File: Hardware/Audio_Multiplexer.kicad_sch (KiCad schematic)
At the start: 1 part

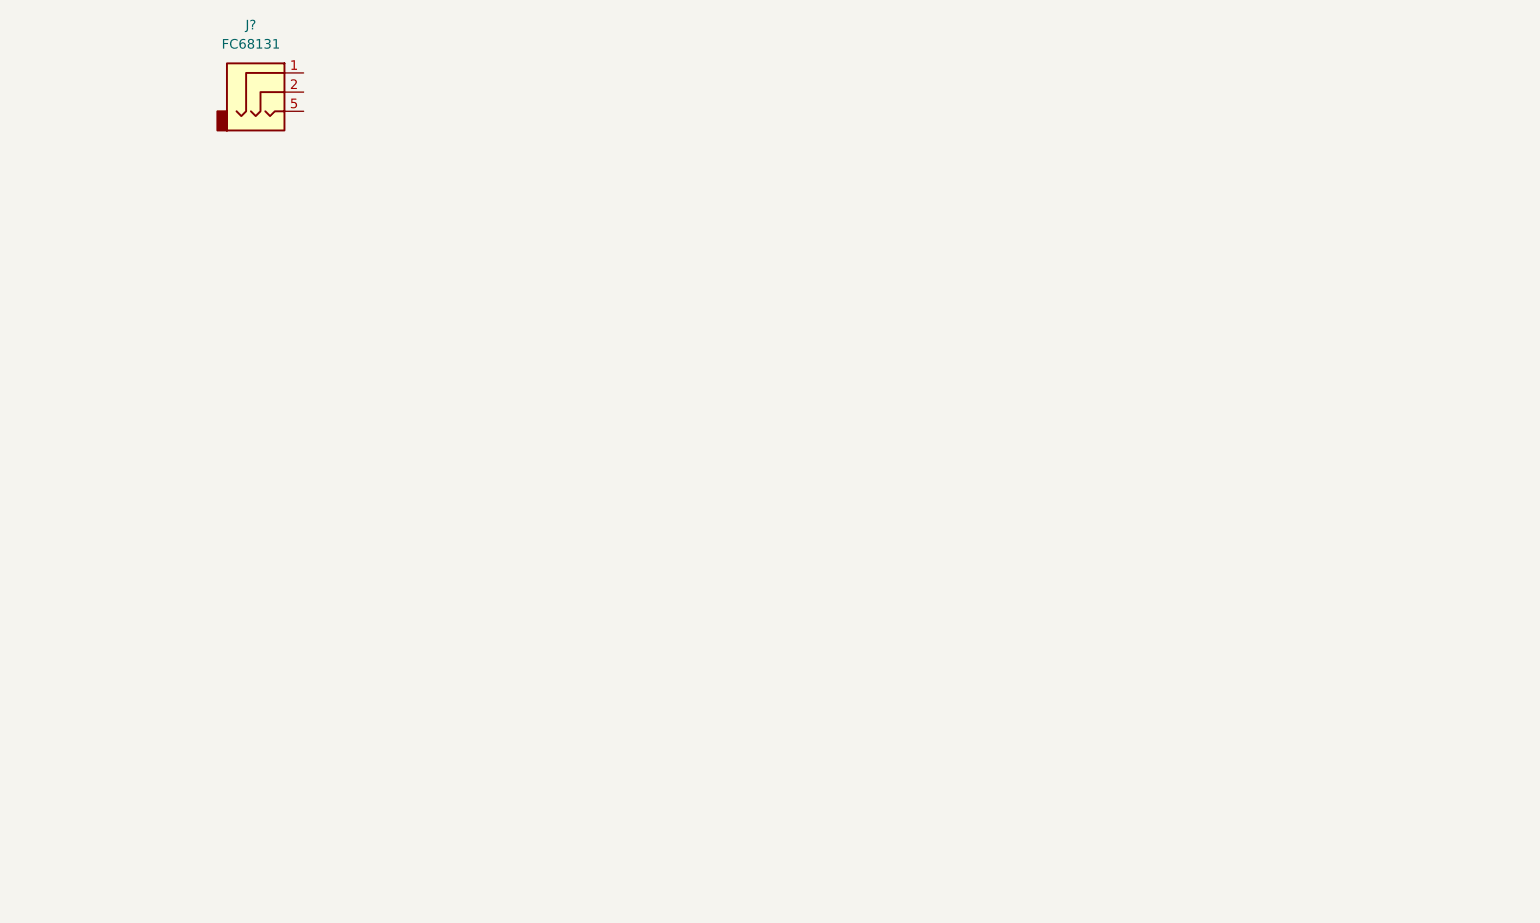
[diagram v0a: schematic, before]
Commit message: Finished schematic. Added audio and microphone blocks.
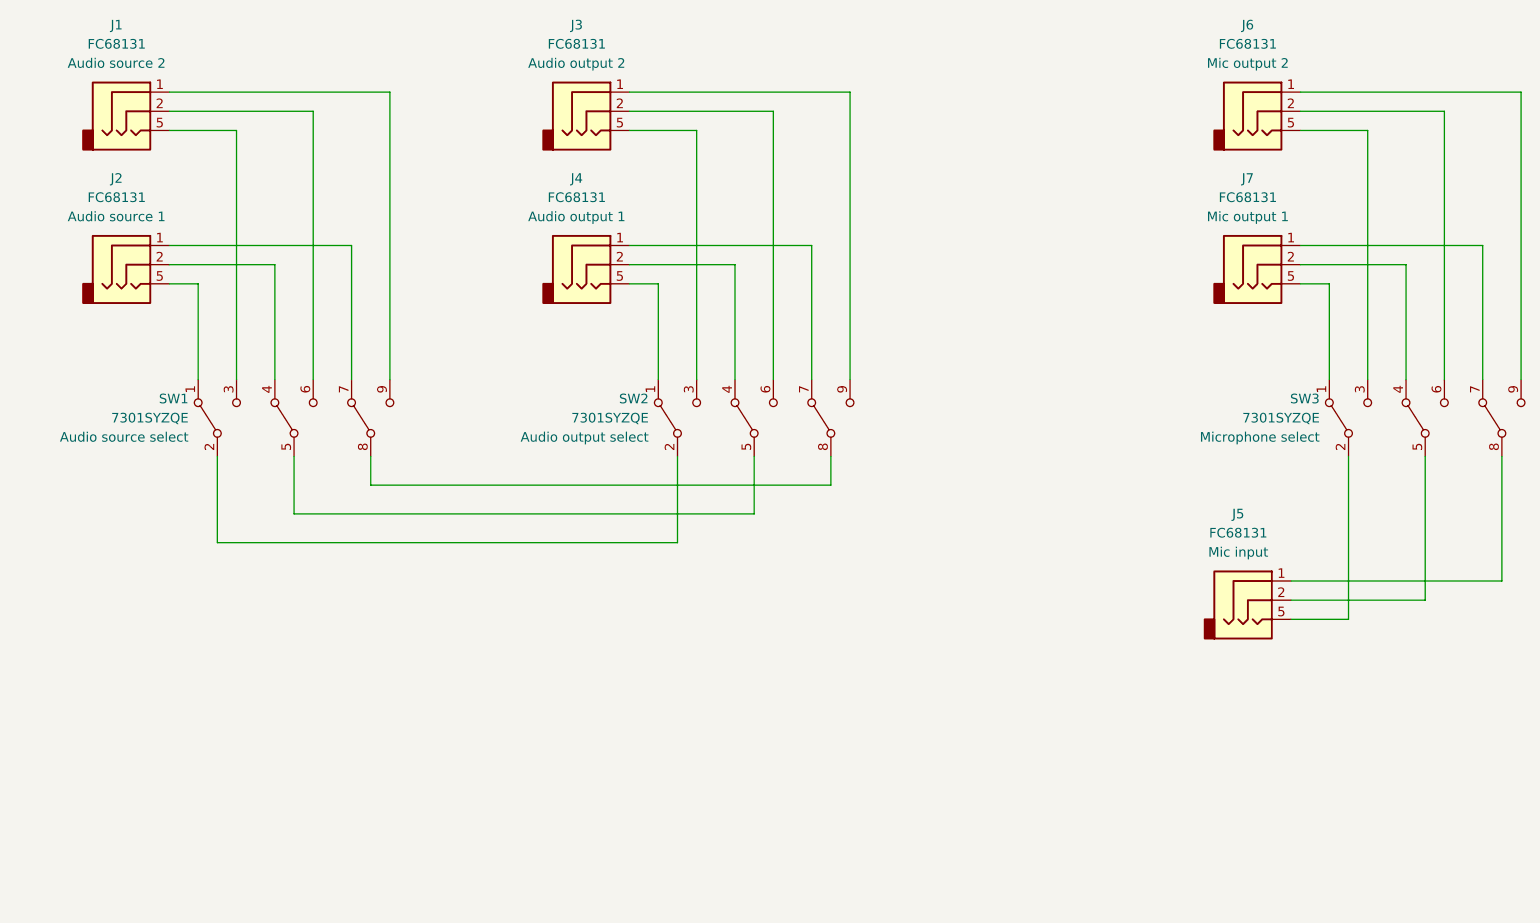
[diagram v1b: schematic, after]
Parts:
- added J1, J3, J4, J5, J6, J7: FC68131, FC68131:FC68131, symbol FC68131:FC68131
- added SW1, SW2, SW3: 7301SYZQE, 7301SYZQE:7301SYZQE, symbol 7301SYZQE:7301SYZQE
- gave numbers to parts that had none: 1
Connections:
- net at J2.1: now also SW1.7
- net at J2.2: now also SW1.4
- net at J2.5: now also SW1.1
- new net: J7.1, SW3.7
- new net: J7.2, SW3.4
- new net: J7.5, SW3.1
- new net: J4.1, SW2.7
- new net: J4.2, SW2.4
- new net: J4.5, SW2.1
- new net: J6.1, SW3.9
- new net: J6.2, SW3.6
- new net: J6.5, SW3.3
- new net: J3.1, SW2.9
- new net: J3.2, SW2.6
- new net: J3.5, SW2.3
- new net: J5.5, SW3.2
- new net: J5.2, SW3.5
- new net: J5.1, SW3.8
- new net: SW1.2, SW2.2
- new net: J1.5, SW1.3
- new net: SW1.5, SW2.5
- new net: J1.2, SW1.6
- new net: SW1.8, SW2.8
- new net: J1.1, SW1.9
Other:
- company: (none) -> (C) Adrien RICCIARDI
- title: (none) -> Audio multiplexer
- moved on the sheet: J2

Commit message: Placed all components and routed the circuit.
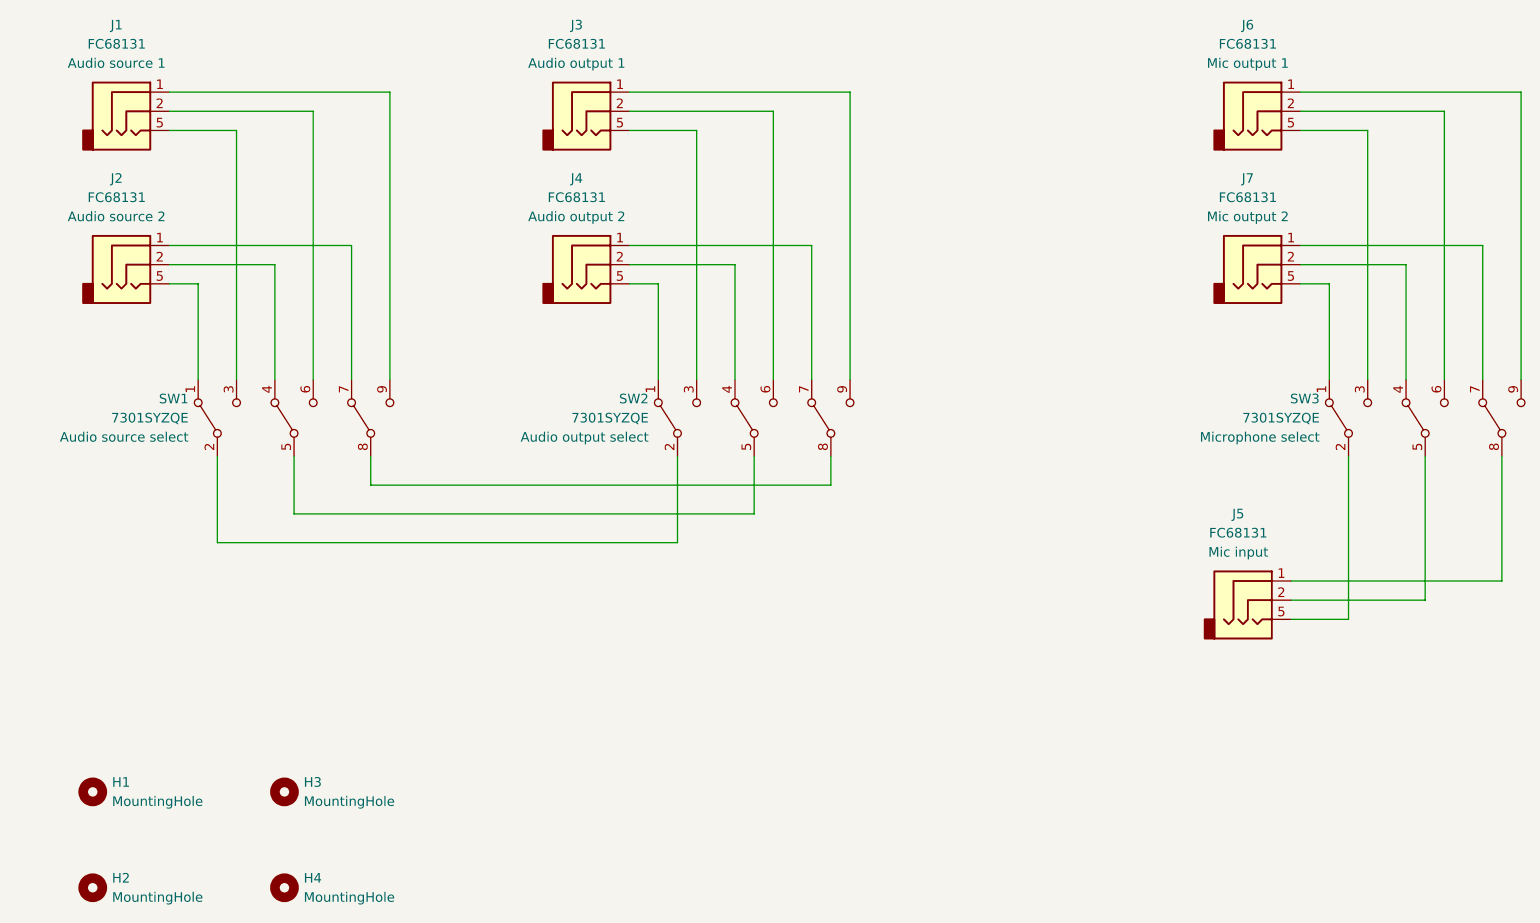
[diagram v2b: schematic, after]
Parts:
- added H1, H2, H3, H4: MountingHole, MountingHole:MountingHole_4.5mm, symbol Mechanical:MountingHole
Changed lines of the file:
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@@
       (effects (font (size 1.27 1.27)) hide)
     )
-    (property "Description" "Mic output 1" (id 4) (at 203.835 76.2 0))
-    (pin "1")
-    (pin "2")
-    (pin "5")
+    (property "Description" "Mic output 2" (id 4) (at 203.835 76.2 0))
+    (pin "1")
+    (pin "2")
+    (pin "5")
+  )
+  (symbol (lib_id "Mechanical:MountingHole") (at 50.8 152.4 0) (unit 1)
+    (in_bom yes) (on_board yes) (fields_autoplaced)
+    (property "Reference" "H1" (id 0) (at 53.34 151.1299 0)
+      (effects (font (size 1.27 1.27)) (justify left))
+    )
+    (property "Value" "MountingHole" (id 1) (at 53.34 153.6699 0)
+      (effects (font (size 1.27 1.27)) (justify left))
+    )
+    (property "Footprint" "MountingHole:MountingHole_4.5mm" (id 2) (at 50.8 152.4 0)
+      (effects (font (size 1.27 1.27)) hide)
+    )
+    (property "Datasheet" "~" (id 3) (at 50.8 152.4 0)
+      (effects (font (size 1.27 1.27)) hide)
+    )
   )
   (symbol (lib_id "FC68131:FC68131") (at 116.84 82.55 0) (unit 1)
@@
       (effects (font (size 1.27 1.27)) hide)
     )
-    (property "Description" "Audio output 1" (id 4) (at 114.935 76.2 0))
+    (property "Description" "Audio output 2" (id 4) (at 114.935 76.2 0))
     (pin "1")
     (pin "2")
@@
       (effects (font (size 1.27 1.27)) hide)
     )
-    (property "Description" "Mic output 2" (id 4) (at 203.835 55.88 0))
+    (property "Description" "Mic output 1" (id 4) (at 203.835 55.88 0))
     (pin "1")
     (pin "2")
@@
       (effects (font (size 1.27 1.27)) hide)
     )
-    (property "Description" "Audio source 1" (id 4) (at 53.975 76.2 0))
+    (property "Description" "Audio source 2" (id 4) (at 53.975 76.2 0))
     (pin "1")
     (pin "2")
@@
       (effects (font (size 1.27 1.27)) hide)
     )
-    (property "Description" "Audio output 2" (id 4) (at 114.935 55.88 0))
+    (property "Description" "Audio output 1" (id 4) (at 114.935 55.88 0))
     (pin "1")
     (pin "2")
@@
     (pin "9")
   )
+  (symbol (lib_id "Mechanical:MountingHole") (at 50.8 165.1 0) (unit 1)
+    (in_bom yes) (on_board yes) (fields_autoplaced)
+    (property "Reference" "H2" (id 0) (at 53.34 163.8299 0)
+      (effects (font (size 1.27 1.27)) (justify left))
+    )
+    (property "Value" "MountingHole" (id 1) (at 53.34 166.3699 0)
+      (effects (font (size 1.27 1.27)) (justify left))
+    )
+    (property "Footprint" "MountingHole:MountingHole_4.5mm" (id 2) (at 50.8 165.1 0)
+      (effects (font (size 1.27 1.27)) hide)
+    )
+    (property "Datasheet" "~" (id 3) (at 50.8 165.1 0)
+      (effects (font (size 1.27 1.27)) hide)
+    )
+  )
   (symbol (lib_name "7301SYZQE_1") (lib_id "7301SYZQE:7301SYZQE") (at 77.47 102.87 90) (unit 1)
     (in_bom yes) (on_board yes) (fields_autoplaced)
@@
     (pin "9")
   )
+  (symbol (lib_id "Mechanical:MountingHole") (at 76.2 165.1 0) (unit 1)
+    (in_bom yes) (on_board yes) (fields_autoplaced)
+    (property "Reference" "H4" (id 0) (at 78.74 163.8299 0)
+      (effects (font (size 1.27 1.27)) (justify left))
+    )
+    (property "Value" "MountingHole" (id 1) (at 78.74 166.3699 0)
+      (effects (font (size 1.27 1.27)) (justify left))
+    )
+    (property "Footprint" "MountingHole:MountingHole_4.5mm" (id 2) (at 76.2 165.1 0)
+      (effects (font (size 1.27 1.27)) hide)
+    )
+    (property "Datasheet" "~" (id 3) (at 76.2 165.1 0)
+      (effects (font (size 1.27 1.27)) hide)
+    )
+  )
   (symbol (lib_id "FC68131:FC68131") (at 55.88 62.23 0) (unit 1)
     (in_bom yes) (on_board yes) (fields_autoplaced)
@@
       (effects (font (size 1.27 1.27)) hide)
     )
-    (property "Description" "Audio source 2" (id 4) (at 53.975 55.88 0))
+    (property "Description" "Audio source 1" (id 4) (at 53.975 55.88 0))
     (pin "1")
     (pin "2")
@@
     (pin "9")
   )
+  (symbol (lib_id "Mechanical:MountingHole") (at 76.2 152.4 0) (unit 1)
+    (in_bom yes) (on_board yes) (fields_autoplaced)
+    (property "Reference" "H3" (id 0) (at 78.74 151.1299 0)
+      (effects (font (size 1.27 1.27)) (justify left))
+    )
+    (property "Value" "MountingHole" (id 1) (at 78.74 153.6699 0)
+      (effects (font (size 1.27 1.27)) (justify left))
+    )
+    (property "Footprint" "MountingHole:MountingHole_4.5mm" (id 2) (at 76.2 152.4 0)
+      (effects (font (size 1.27 1.27)) hide)
+    )
+    (property "Datasheet" "~" (id 3) (at 76.2 152.4 0)
+      (effects (font (size 1.27 1.27)) hide)
+    )
+  )
   (sheet_instances
     (path "/" (page "1"))
   )
   (symbol_instances
+    (path "/195d5691-68ca-4e91-af9b-faa298eb034c"
+      (reference "H1") (unit 1) (value "MountingHole") (footprint "MountingHole:MountingHole_4.5mm")
+    )
+    (path "/a36f052f-2e65-4f72-80e6-18baa15f7121"
+      (reference "H2") (unit 1) (value "MountingHole") (footprint "MountingHole:MountingHole_4.5mm")
+    )
+    (path "/ed6ba90c-026e-487c-8385-6cffd6d808ba"
+      (reference "H3") (unit 1) (value "MountingHole") (footprint "MountingHole:MountingHole_4.5mm")
+    )
+    (path "/bae3a5e2-9800-4b44-a671-bec3722e0b63"
+      (reference "H4") (unit 1) (value "MountingHole") (footprint "MountingHole:MountingHole_4.5mm")
+    )
     (path "/bfb1f504-f01f-4fb4-8d06-be041ed9429b"
       (reference "J1") (unit 1) (value "FC68131") (footprint "FC68131:FC68131")
